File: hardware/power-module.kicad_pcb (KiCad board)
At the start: 4 copper layers, 85 x 50 mm, 86 parts, among them CN1 WJ2EDGRC-5.08-2P, J1 Conn_01x04_Pin, J2 Conn_01x02, J3 Conn_01x02, J4 Conn_01x02, K1 SRA-12VDC-CL, K2 SRA-12VDC-CL, K3 SRA-12VDC-CL, K4 SRA-12VDC-CL, P1 WJ2EDGRC-5.08-4P, Q1 SS8050_C2150, Q2 SS8050_C2150, U1 AMS1117-3.3_C347222, U10 XL-1010RGBC-WS2812B, U11 XL-1010RGBC-WS2812B, U12 XL-1010RGBC-WS2812B, U13 L327S400H11L, U14 UMW78L05, U15 XL-1010RGBC-WS2812B, U16 XL-1010RGBC-WS2812B, U17 XL-1010RGBC-WS2812B, U18 XL-1010RGBC-WS2812B, U2 CC6903SO-10A, U3 W5500, U4 ESP32-C3FH4, U5 AMS1117-3.3_C347222, U6 XL-1010RGBC-WS2812B, U7 DP9900LP-12V, U8 XL-1010RGBC-WS2812B, U9 XL-1010RGBC-WS2812B, X1 X322525MRB4SI

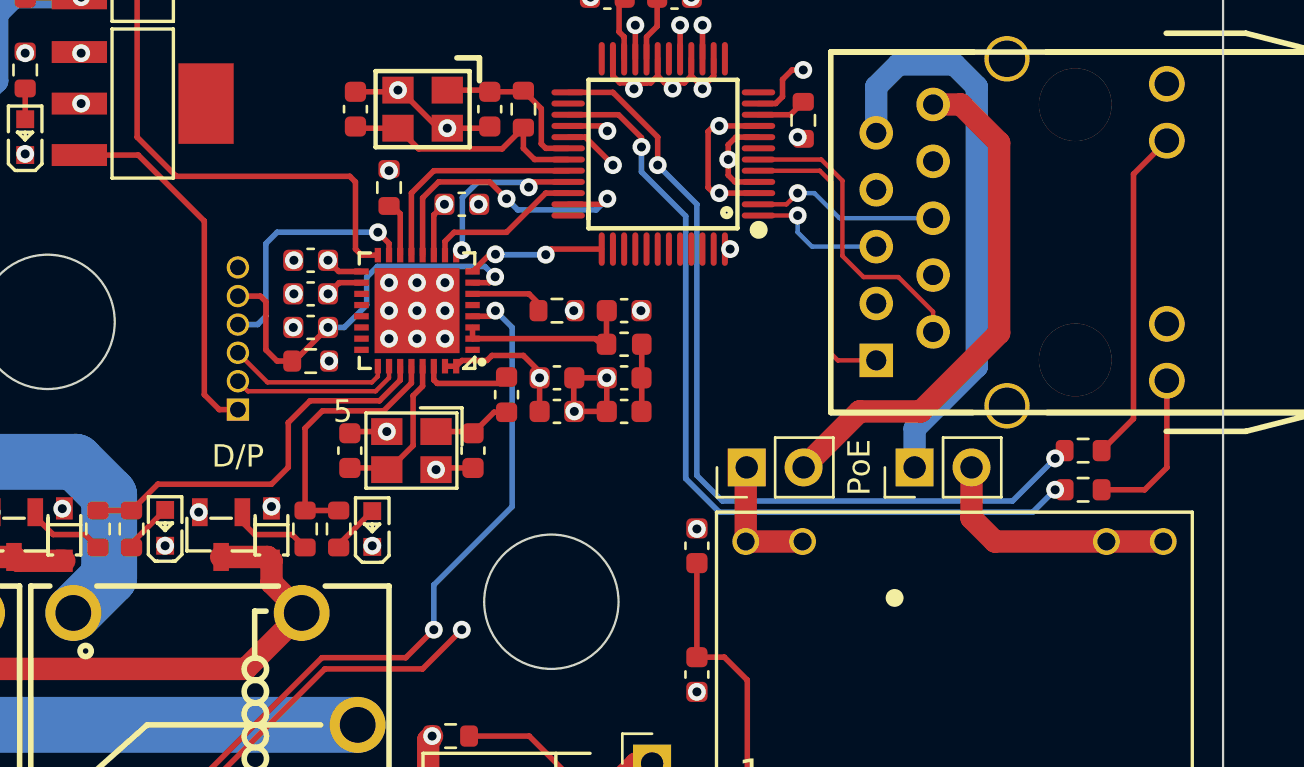
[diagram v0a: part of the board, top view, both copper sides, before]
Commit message: Add current sensing input capactior
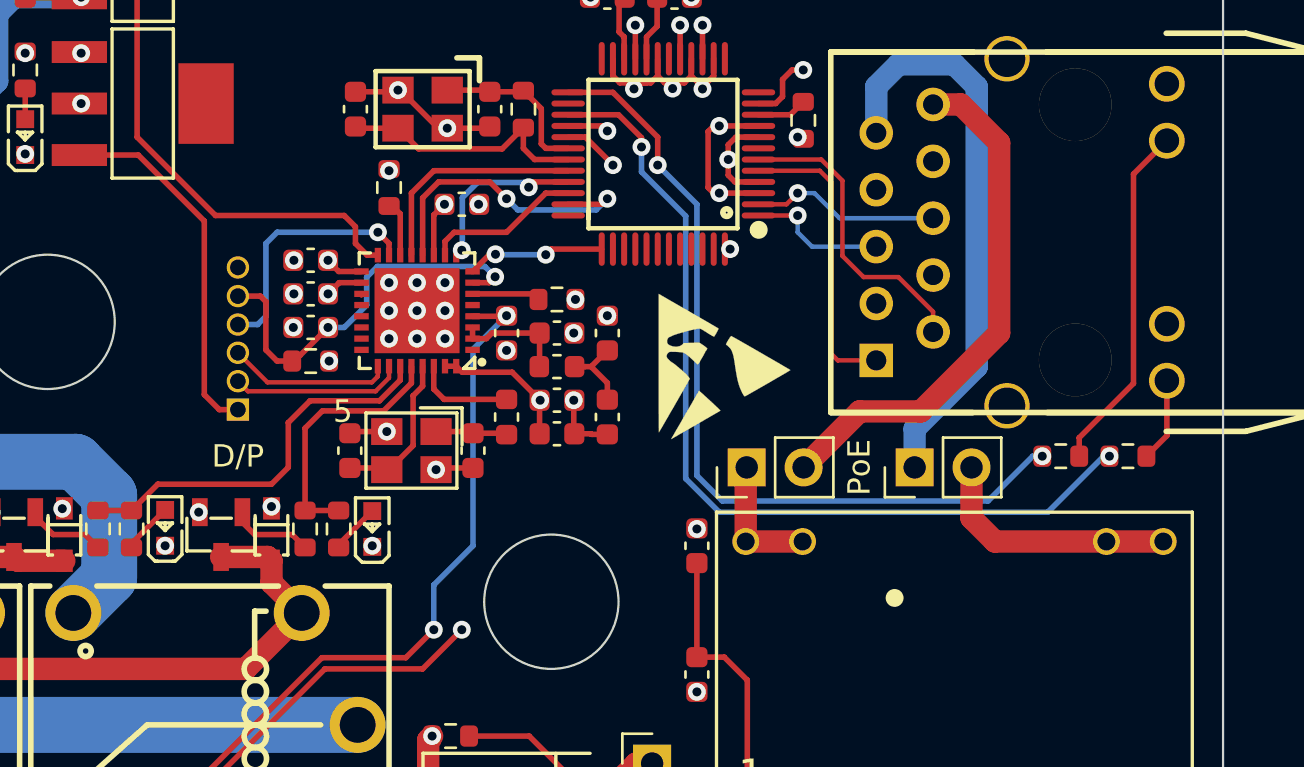
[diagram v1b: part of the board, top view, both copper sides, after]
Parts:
- added C34: 0.1uF, Capacitor_SMD:C_0603_1608Metric, F.Cu at (53.0, 25.5)
- added REF**: ESD-Logo_6.6x6mm_SilkScreen, Symbol:ESD-Logo_6.6x6mm_SilkScreen, F.Cu at (62.8, 27.0)
- added REF**: OSHW-Symbol_6.7x6mm_SilkScreen, Symbol:OSHW-Symbol_6.7x6mm_SilkScreen, B.Cu at (46.0, 30.2)
- moved C25 3.16 mm to (55.2, 25.5)
- moved L1 3.16 mm to (55.2, 27.0)
- moved R2 2.50 mm to (80.8, 31.0)
- moved C26 2.14 mm to (57.5, 25.5), turned to -90 degrees
- moved R4 1.03 mm to (77.8, 31.0)
- moved C21 1.00 mm to (55.2, 30.0)
- moved C22 1.00 mm to (55.2, 28.5)
- moved L2 1.00 mm to (53.0, 29.2)
- moved C27 0.79 mm to (57.5, 29.2), turned to 90 degrees
- moved R8 0.50 mm to (55.2, 24.0)
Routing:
- net Net-(R2-Pad1): track 7.21 -> 3.75 mm
- net Net-(C25-Pad2): track 8.44 -> 5.12 mm
- net GND: track 65.2 -> 62.4 mm, vias 65 -> 66
- net /LED ACTIVITY: track 37.7 -> 40.3 mm
- net /LED DATA IN: track 43.8 -> 42.4 mm
- net /LED LINK: track 38.5 -> 37.4 mm
- net Net-(R4-Pad1): track 15.0 -> 15.7 mm
- net Net-(C26-Pad2): track 3.01 -> 3.56 mm
